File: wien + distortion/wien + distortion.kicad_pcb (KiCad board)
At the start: 2 copper layers, 51 x 36 mm, 47 parts, among them J1 INPUT, J2 OUTPUT, J3 PWR switch, J4 OUTPUT, J5 Conn_01x01_Pin, U1 NE5532, U2 NE5532, U3 NE5532

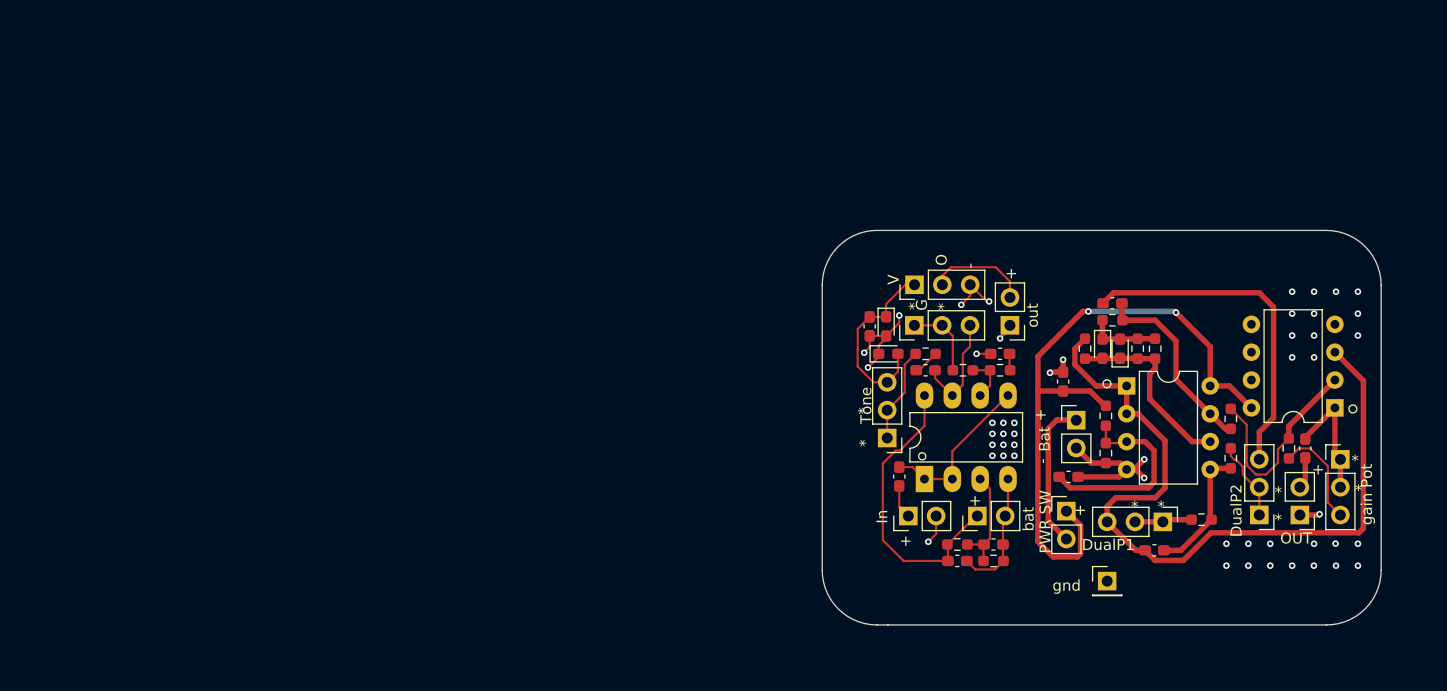
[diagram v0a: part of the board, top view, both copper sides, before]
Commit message: decided to use one power supply for both circuits so redid the pcb to reflect that
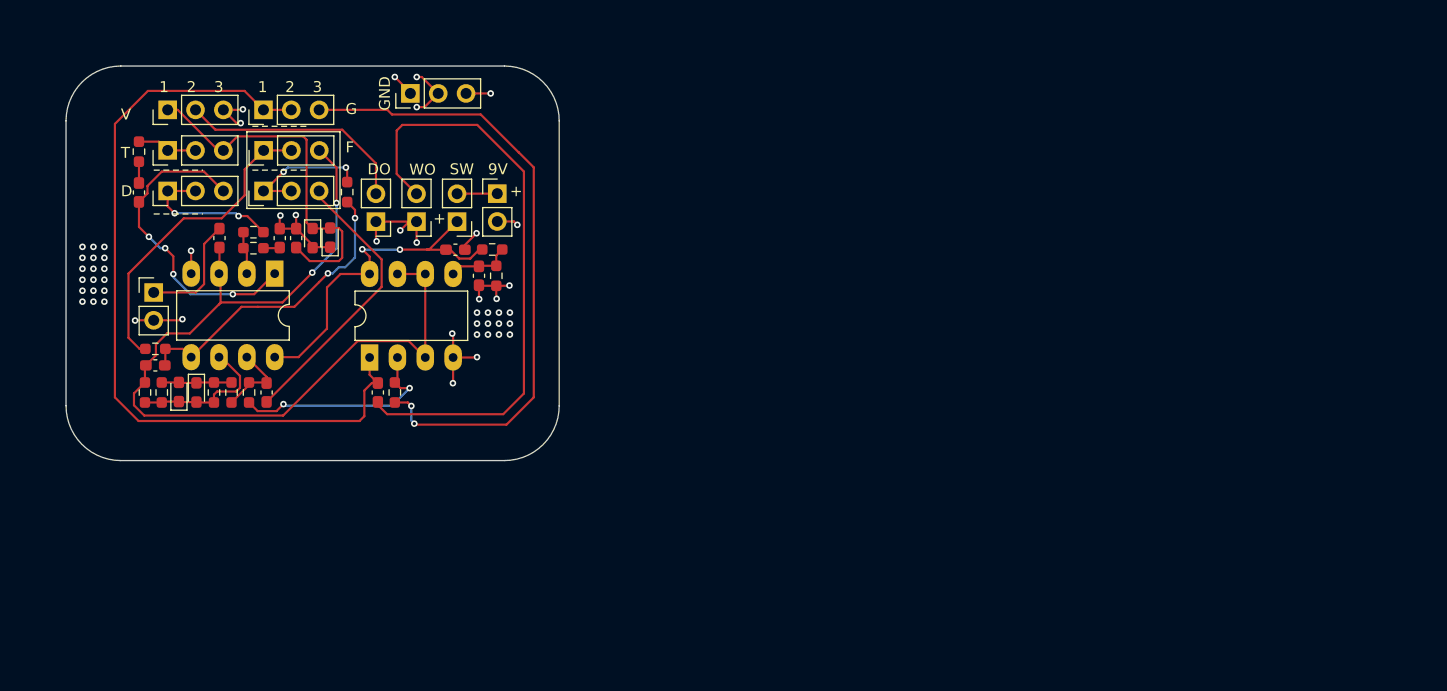
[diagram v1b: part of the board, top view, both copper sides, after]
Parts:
- removed the BT1 at (135.2, 116.1)
- removed the C1 at (133.3, 120.2)
- removed the C2 at (136.6, 118.7)
- removed the J5 at (147.0, 122.0)
- removed the R1 at (133.3, 118.7)
- removed the R2 at (136.6, 120.2)
- removed U3: NE5532, Package_DIP:DIP-8_W7.62mm
- added GND: GND connections, Connector_PinHeader_2.54mm:PinHeader_1x03_P2.54mm_Vertical, F.Cu at (83.4, 77.5)
- RV1: value 20k? -> 20k? tone
- U2: footprint Package_DIP:DIP-8_W7.62mm -> Package_DIP:DIP-8_W7.62mm_LongPads
- moved RV5 103.3 mm to (70.0, 79.0), turned to 90 degrees
- moved R10 96.7 mm to (60.1, 100.8)
- moved RV4 95.6 mm to (70.0, 86.4), turned to 90 degrees
- moved C7 92.7 mm to (60.1, 102.3)
- moved R12 89.6 mm to (68.7, 104.8), turned to -90 degrees
- moved R5 89.1 mm to (60.7, 104.8)
- moved G*** 88.8 mm to (56.4, 102.1), turned to 180 degrees
- moved DualPot1 88.8 mm to (70.0, 82.7), turned to 90 degrees
- moved R4 86.0 mm to (65.5, 104.8)
- moved D3 86.0 mm to (62.3, 104.7)
- moved R6 85.9 mm to (59.2, 104.8)
- moved J5 84.9 mm to (84.0, 89.2)
- moved C8 84.8 mm to (80.5, 104.8)
- moved R8 84.2 mm to (77.7, 86.5)
- moved D4 82.8 mm to (63.9, 104.8)
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- renumbered BT2 to BT1, C3 to C1, C4 to C2, C5 to C3, C6 to C4, C7 to C5, C8 to C6, C9 to C7, C10 to C8, C11 to C9, J3 to J4, J4 to J5, R3 to R1, R12 to R10, R13 to R11, R14 to R12, R15 to R13, R4 to R2, R5 to R3, R6 to R4, R7 to R5, R8 to R6, R9 to R7, R10 to R8, R11 to R9
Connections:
- C1 pad 2: Net-(U1A--) -> BiasVoltage
- C2 pad 1: Net-(C4-Pad1) -> Net-(C2-Pad1)
- C5 pad 1: Net-(C7-Pad1) -> Net-(C5-Pad1)
- C5 pad 2: Net-(C7-Pad2) -> Net-(C5-Pad2)
- C7 pad 1: Net-(U2B-+) -> Net-(U1B-+)
- C8 pad 1: Net-(C10-Pad1) -> Net-(C8-Pad1)
- C9 pad 1: Net-(U2A-+) -> Net-(U2B-+)
- R10 pad 2: Net-(U2B-+) -> Net-(U1B-+)
- R11 pad 1: Net-(U2A-+) -> Net-(U2B-+)
- R12 pad 1: Net-(C7-Pad2) -> Net-(C5-Pad1)
- R12 pad 2: Net-(U3A--) -> Net-(U2A--)
- R13 pad 1: Net-(U3A--) -> Net-(U2A--)
- R2 pad 2: Net-(U1B--) -> Net-(U1A--)
- R3 pad 1: Net-(U1B--) -> Net-(U1A--)
- R7 pad 2: Net-(C7-Pad2) -> Net-(C5-Pad1)
- R8 pad 1: Net-(U2B-+) -> Net-(U1B-+)
- R9 pad 2: Net-(U2A-+) -> Net-(U2B-+)
- RV3 pad 3: Net-(C4-Pad1) -> Net-(C2-Pad1)
- RV4 pad 3: Net-(C7-Pad1) -> Net-(C5-Pad2)
- RV5 pad 1: Net-(C10-Pad1) -> Net-(C8-Pad1)
- RV5 pad 2: Net-(C10-Pad1) -> Net-(C8-Pad1)
- U1 pad 1: Net-(U1A--) -> Net-(C2-Pad1)
- U1 pad 3: Net-(U1A-+) -> BiasVoltage
- U1 pad 4: Net-(BT1--) -> GND
- U1 pad 5: Net-(U1A--) -> Net-(U1B-+)
- U1 pad 6: Net-(U1B--) -> Net-(D3-K)
- U1 pad 7: Net-(C4-Pad1) -> Net-(C5-Pad1)
- U1 pad 8: Net-(BT1-+) (its old number) -> +9V
- U2 pad 1: BiasVoltage -> Net-(C8-Pad1)
- U2 pad 2: BiasVoltage -> Net-(U2A--)
- U2 pad 3: Net-(U2A-+) -> BiasVoltage
- U2 pad 6: Net-(D3-K) -> BiasVoltage
- U2 pad 7: Net-(C7-Pad2) -> BiasVoltage
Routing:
- net Net-(C8-Pad1): track 0.00 -> 73.3 mm
- net Net-(J5-Pin_2): track 2.88 -> 55.1 mm
- net Net-(R13-Pad2): track 9.55 -> 58.1 mm, vias 0 -> 2
- net Net-(C7-Pad1): track 30.9 -> 0.00 mm
- net Net-(C2-Pad1): track 0.00 -> 29.8 mm, vias 0 -> 4
- net Net-(U1B-+): track 0.00 -> 28.3 mm, vias 0 -> 2
- net Net-(BT1-+) (its old number): track 27.8 -> 0.00 mm
- net +9V: track 59.6 -> 32.0 mm
- net Net-(C5-Pad2): track 0.00 -> 26.0 mm
- net Net-(DualPot1-Pad1): track 5.52 -> 28.7 mm
- net Net-(U2A--): track 0.00 -> 20.0 mm, vias 0 -> 2
- net Net-(U3A--): track 19.1 -> 0.00 mm
- net Net-(U2A-+): track 18.6 -> 0.00 mm
- net Net-(C7-Pad2): track 17.6 -> 0.00 mm
- net Net-(D1-K): track 17.3 -> 33.3 mm
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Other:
- board size 51 x 36 mm -> 45 x 36 mm
- board text added: "1"
- board text added: "2"
- board text added: "3"
- board text added: "9V"
- board text added: "D"
- board text added: "DO"
- board text added: "F"
- board text added: "SW"
- board text added: "T"
- board text added: "WO"
- board text removed: "*"
- board text removed: "-"
- board text removed: "Bat"
- board text removed: "DualP1"
- board text removed: "DualP2"
- board text removed: "In"
- board text removed: "O"
- board text removed: "OUT"
- board text removed: "PWR SW"
- board text removed: "Tone"
- board text removed: "bat"
- board text removed: "gain Pot"
- board text removed: "gnd"
- board text removed: "out"

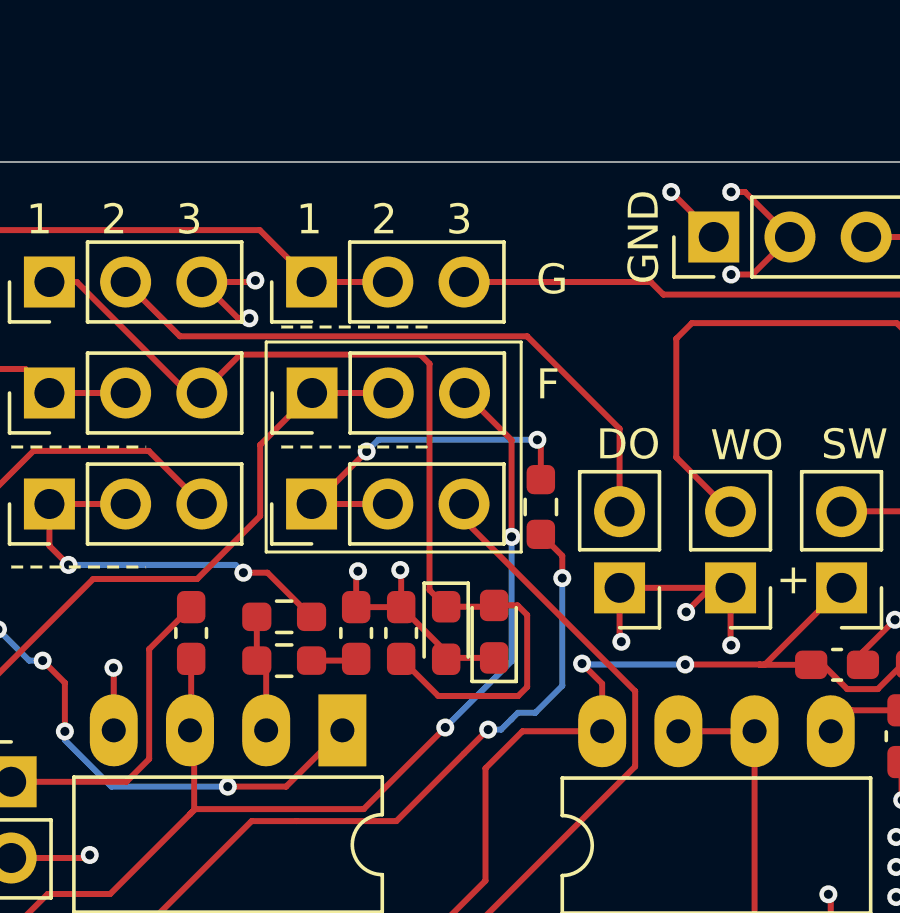
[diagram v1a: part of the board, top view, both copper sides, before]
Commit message: changed diodes to sod-123 package and changed pcb accordingly and create gerber,drill, pos,and BOM list for manufacturing
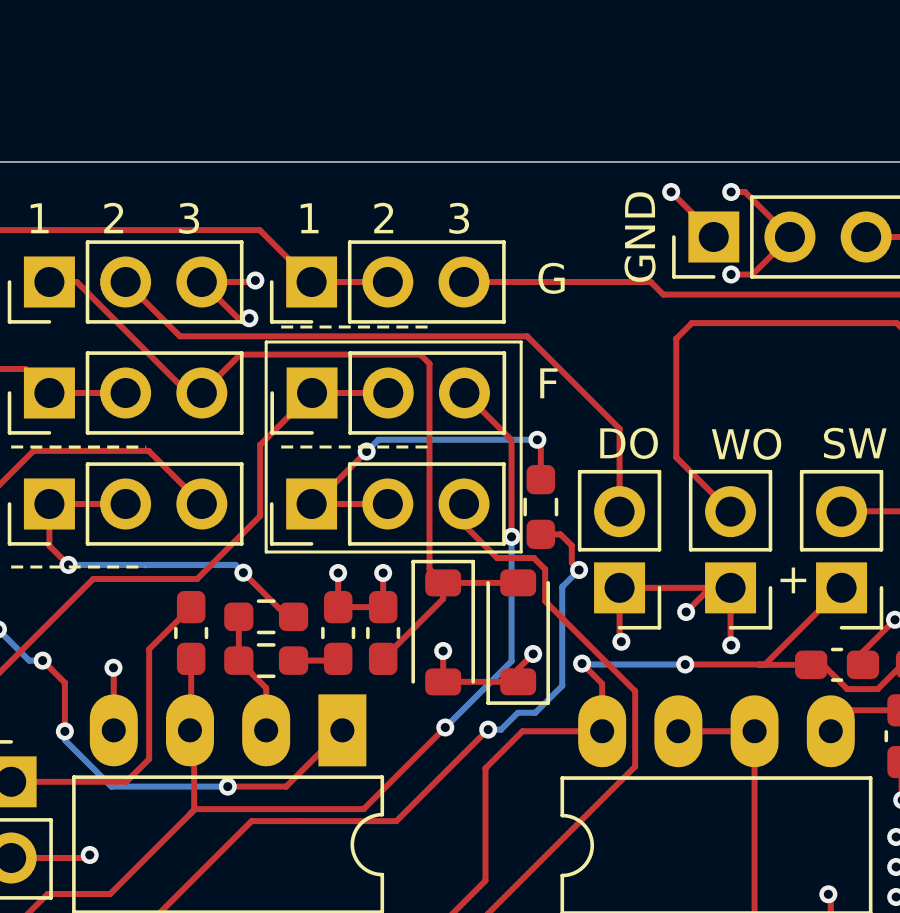
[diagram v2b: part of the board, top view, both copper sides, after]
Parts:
- D1, D2: footprint Diode_SMD:D_0603_1608Metric_Pad1.05x0.95mm_HandSolder -> Diode_SMD:D_SOD-123
- moved D2 0.80 mm to (76.9, 90.7)
- moved C3 0.60 mm to (70.9, 90.7)
- moved C4 0.60 mm to (72.4, 90.7)
- moved R2 0.60 mm to (68.5, 91.6)
- moved R3 0.60 mm to (68.5, 90.2)
- moved D1 0.10 mm to (74.4, 90.7)
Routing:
- net Net-(D1-K): track 33.3 -> 28.1 mm
- net Net-(U1B-+): track 28.3 -> 29.1 mm
- net Net-(U1A--): track 3.91 -> 4.67 mm
- net Net-(C5-Pad2): track 26.0 -> 26.7 mm
- net Net-(R3-Pad2): track 13.7 -> 13.1 mm
- net GND: track 52.9 -> 53.4 mm, vias 52 -> 54

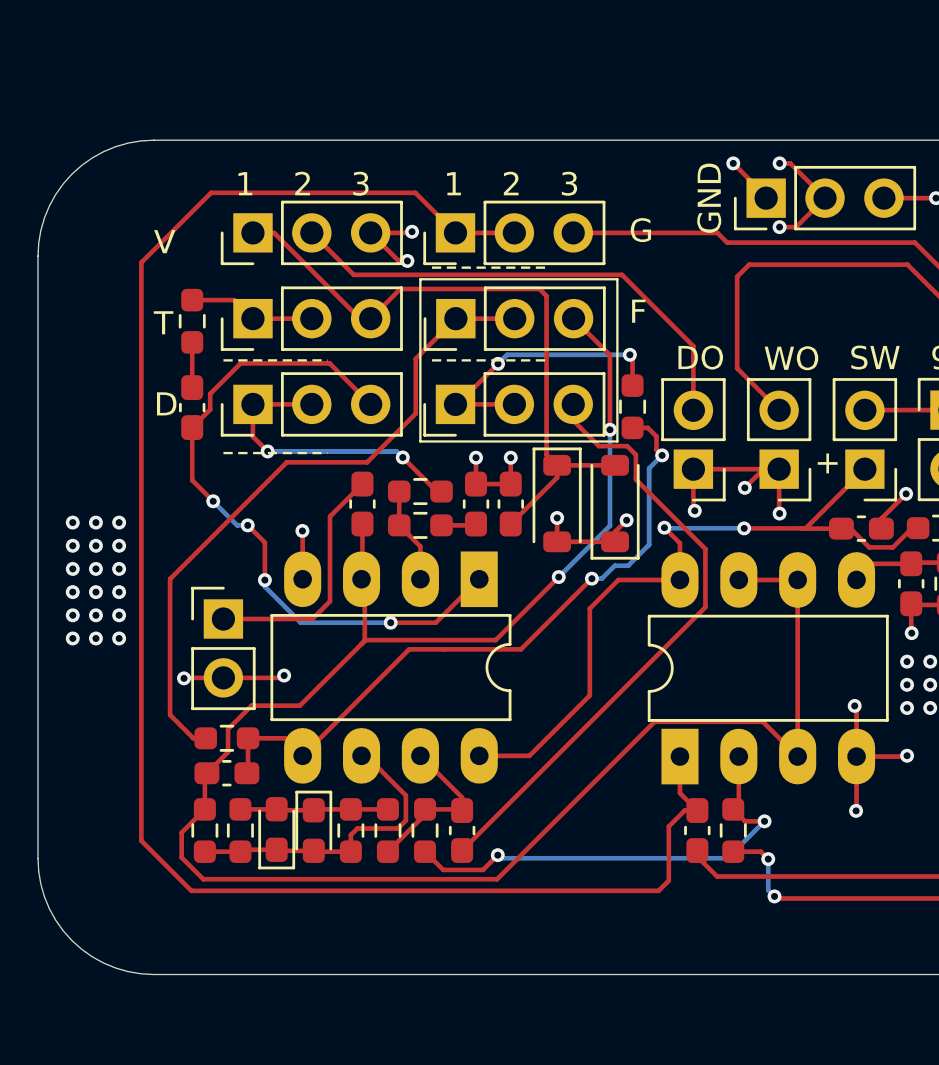
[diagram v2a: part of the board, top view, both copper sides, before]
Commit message: redid the manufacturing files since i had the wrong diode foot print
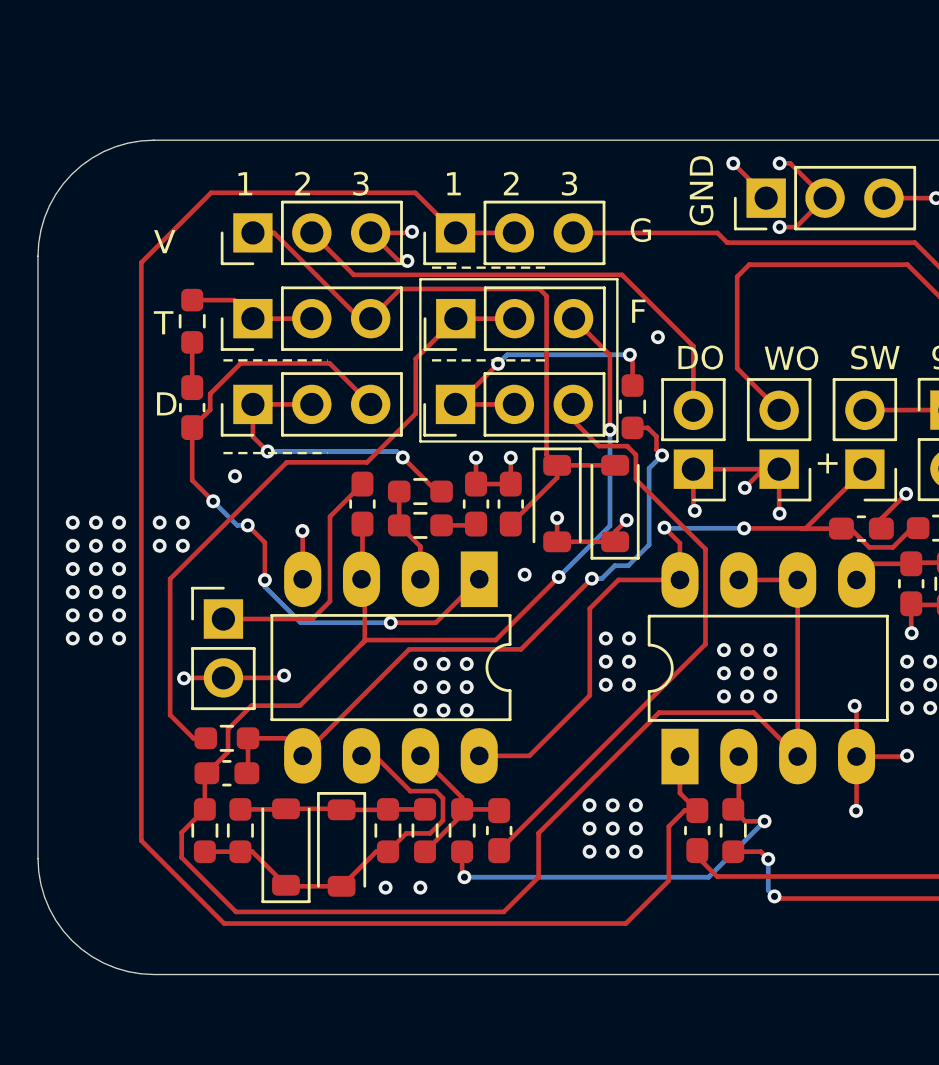
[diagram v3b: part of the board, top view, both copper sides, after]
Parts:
- D3, D4: footprint Diode_SMD:D_0603_1608Metric_Pad1.05x0.95mm_HandSolder -> Diode_SMD:D_SOD-123
- moved C5 1.60 mm to (71.9, 104.8)
- moved R7 1.60 mm to (68.7, 104.8)
- moved R12 1.60 mm to (70.3, 104.8)
- moved R4 1.60 mm to (67.1, 104.8)
- moved D4 1.42 mm to (65.1, 105.5)
- moved D3 0.86 mm to (62.7, 105.5)
- renumbered GND to J6
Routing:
- net Net-(D3-K): track 13.4 -> 17.4 mm
- net BiasVoltage: track 81.9 -> 84.6 mm
- net Net-(D3-A): track 6.40 -> 8.29 mm
- net Net-(C8-Pad1): track 73.3 -> 74.5 mm
- net Net-(U2A--): track 20.0 -> 19.0 mm
- net Net-(C5-Pad2): track 26.7 -> 26.0 mm
- net GND: vias 54 -> 96
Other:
- board text added: "GND"
